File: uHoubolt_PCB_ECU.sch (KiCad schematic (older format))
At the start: 88 parts, among them J1 Power In, J2 Debug, J3 CAN1, J4 CAN2, J5 CAN1, J6 CAN2, U1 SiC431C, U2 TS30041-M050QFNR, U3 MCP1700-3302E, U4 MCP2562FDT-H_SN, U5 MCP2562FDT, U6 STM32G491MET6-LQFP80, U7 ICM-20602, U8 W25Q256JV, X1 TXC-7C

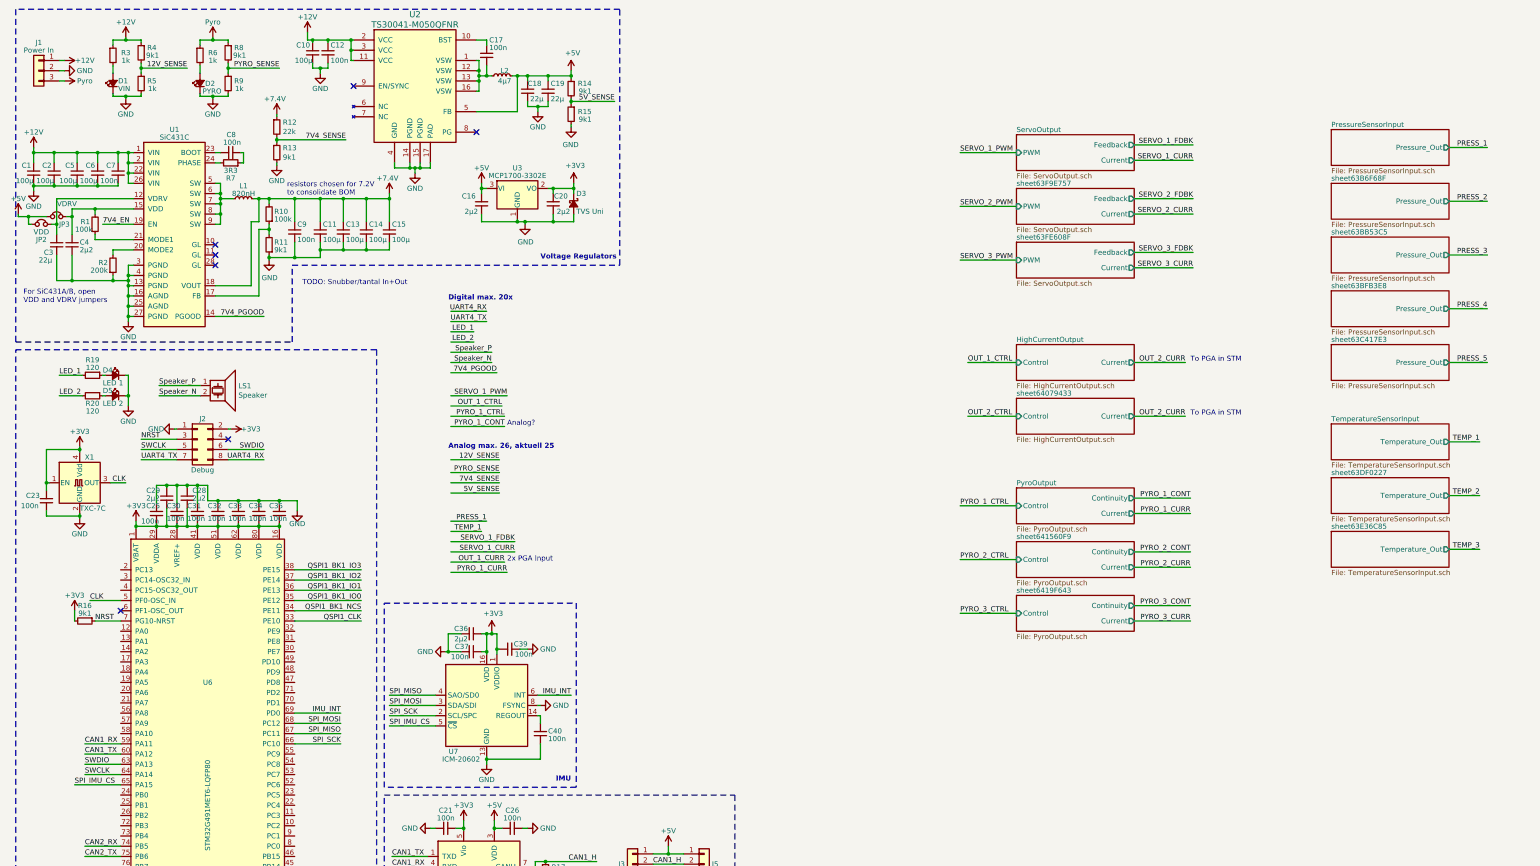
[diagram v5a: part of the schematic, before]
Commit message: moved 7V4 buck to separate board
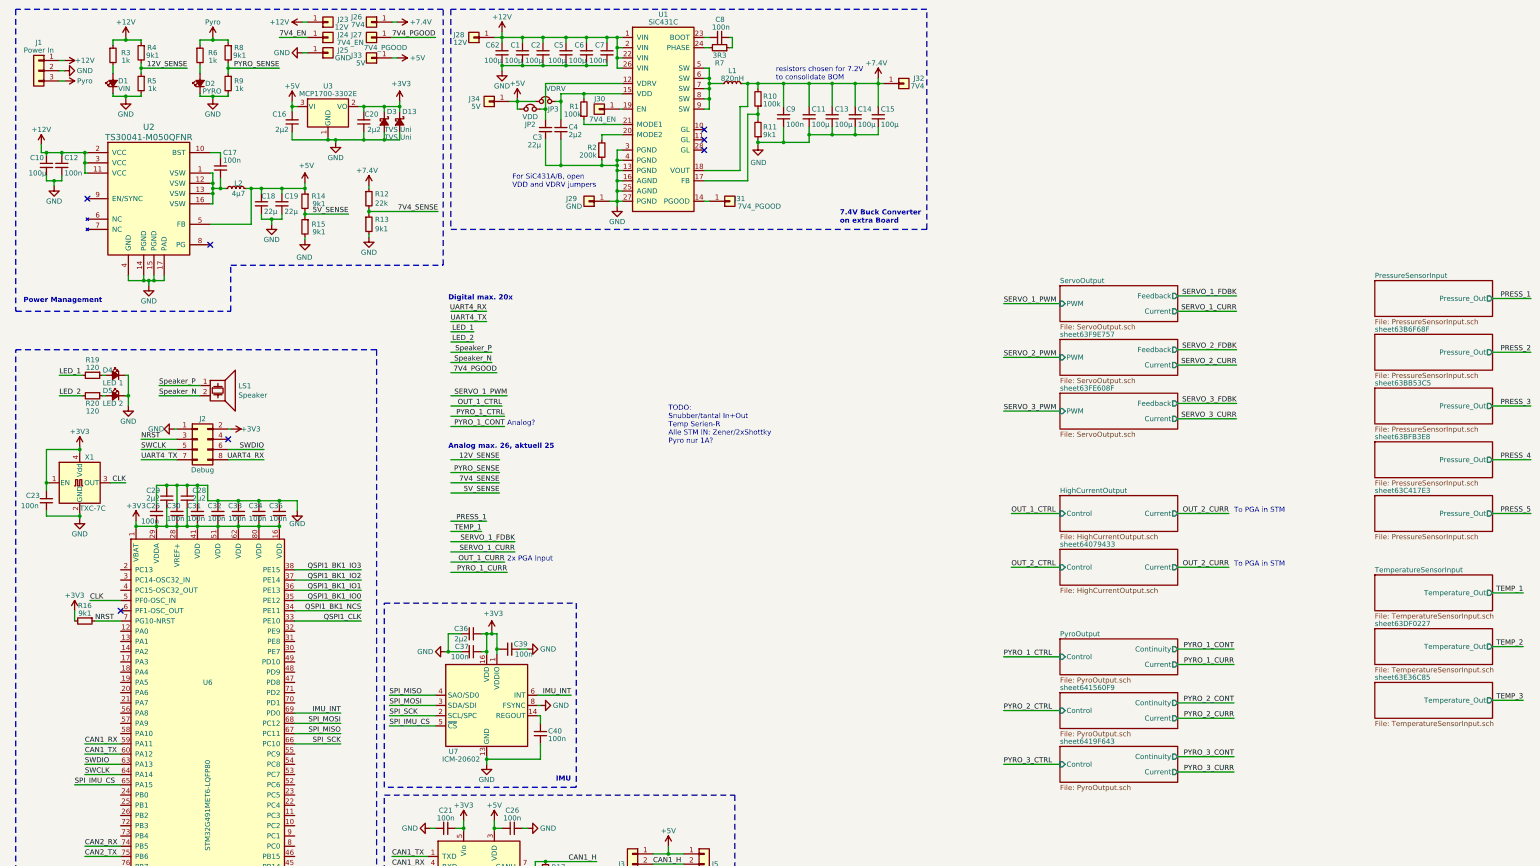
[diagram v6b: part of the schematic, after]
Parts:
- added C62: 100µ, Capacitor_SMD:C_1210_3225Metric, symbol Device:C_Small
- added D13: TVS Uni, TXV_LIB:SOD882D, symbol Device:D_Schottky_Small_ALT
- added J23: 12V, TXV_LIB:PlatedEdgePad_6mm, symbol Connector_Generic:Conn_01x01
- added J24: 7V4_EN, TXV_LIB:PlatedEdgePad_3mm, symbol Connector_Generic:Conn_01x01
- added J25: GND, TXV_LIB:PlatedEdgePad_6mm, symbol Connector_Generic:Conn_01x01
- added J26: 7V4, TXV_LIB:PlatedEdgePad_6mm, symbol Connector_Generic:Conn_01x01
- added J27: 7V4_PGOOD, TXV_LIB:PlatedEdgePad_3mm, symbol Connector_Generic:Conn_01x01
- added J28: 12V, TXV_LIB:PlatedEdge_6mm, symbol Connector_Generic:Conn_01x01
- added J29: GND, TXV_LIB:PlatedEdge_6mm, symbol Connector_Generic:Conn_01x01
- added J30: 7V4_EN, TXV_LIB:PlatedEdge_3mm, symbol Connector_Generic:Conn_01x01
- added J31: 7V4_PGOOD, TXV_LIB:PlatedEdge_3mm, symbol Connector_Generic:Conn_01x01
- added J32: 7V4, TXV_LIB:PlatedEdge_6mm, symbol Connector_Generic:Conn_01x01
- added J33: 5V, TXV_LIB:PlatedEdgePad_3mm, symbol Connector_Generic:Conn_01x01
- added J34: 5V, TXV_LIB:PlatedEdge_3mm, symbol Connector_Generic:Conn_01x01
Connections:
- wire segments 506 -> 523
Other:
- note added: "7.4V Buck Converter\non extra Board"
- note added: "Power Management"
- note added: "TODO:\nSnubber/tantal In+Out\nTemp Serien-R\nAlle STM IN: Zener/2xShottky\nPyro nur 1A?"
- note removed: "TODO: Snubber/tantal In+Out"
- note removed: "Voltage Regulators"
- moved on the sheet: C1, C10, C11, C12, C13, C14, C15, C16, C17, C18, C19, C2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

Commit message: many small changes, before removing servo buck converter
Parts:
- added F?: <1A, symbol Device:Polyfuse_Small
- added J35, J37: CAN1, Connector_JST:JST_GH_BM04B-GHS-TBT_1x04-1MP_P1.25mm_Vertical, symbol Connector_Generic_MountingPin:Conn_01x04_MountingPin
- added J36, J38: CAN2, Connector_JST:JST_GH_BM04B-GHS-TBT_1x04-1MP_P1.25mm_Vertical, symbol Connector_Generic_MountingPin:Conn_01x04_MountingPin
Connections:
- net labels added: 5V_PGOOD, 5V_unfused
- wire segments 523 -> 580
- no-connect marks 7 -> 6
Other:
- note added: "Analog max. 26, aktuell 22"
- note added: "Digital max. 20, aktuell 19"
- note added: "TODO:\nKleinerer L?\nSnubber/tantal In+Out\nAlle STM IN: 2x Shottky\nAnderer Speaker\n6. Druck?\nServo LEDs?\nLEDs 7V4, 5V, 3V3?\nnach außen gehende 12V Versorgungen absichern (vor Messung)"
- note removed: "Analog max. 26, aktuell 25"
- note removed: "Analog?"
- note removed: "Digital max. 20x"
- note removed: "TODO:\nSnubber/tantal In+Out\nTemp Serien-R\nAlle STM IN: Zener/2xShottky\nPyro nur 1A?"
- moved on the sheet: C21, C22, C23, C25, C26, C27, C28, C29, C30, C31, C32, C33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

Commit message: placement almost done
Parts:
- removed C1, C11, C13, C14, C15, C2, C5, C6, C62: 100µ, Capacitor_SMD:C_1210_3225Metric, symbol Device:C_Small
- removed C3: 22µ, Capacitor_SMD:C_0603_1608Metric, symbol Device:C_Small
- removed C4: 2µ2, Capacitor_SMD:C_0603_1608Metric, symbol Device:C_Small
- removed C7, C8, C9: 100n, Capacitor_SMD:C_0402_1005Metric, symbol Device:C_Small
- removed D3: TVS Uni, Diode_SMD:D_SOD-123F, symbol Device:D_Schottky_Small_ALT
- removed J23: 12V, TXV_LIB:PlatedEdgePad_6mm, symbol Connector_Generic:Conn_01x01
- removed J27: 7V4_PGOOD, TXV_LIB:PlatedEdgePad_3mm, symbol Connector_Generic:Conn_01x01
- removed J28: 12V, TXV_LIB:PlatedEdge_6mm, symbol Connector_Generic:Conn_01x01
- removed J29: GND, TXV_LIB:PlatedEdge_6mm, symbol Connector_Generic:Conn_01x01
- removed J30: 7V4_EN, TXV_LIB:PlatedEdge_3mm, symbol Connector_Generic:Conn_01x01
- removed J31: 7V4_PGOOD, TXV_LIB:PlatedEdge_3mm, symbol Connector_Generic:Conn_01x01
- removed J32: 7V4, TXV_LIB:PlatedEdge_6mm, symbol Connector_Generic:Conn_01x01
- removed J33: 5V, TXV_LIB:PlatedEdgePad_3mm, symbol Connector_Generic:Conn_01x01
- removed J34: 5V, TXV_LIB:PlatedEdge_3mm, symbol Connector_Generic:Conn_01x01
- removed JP2: VDD, Jumper:SolderJumper-2_P1.3mm_Bridged_RoundedPad1.0x1.5mm, symbol Device:Jumper_NC_Small
- removed JP3: VDRV, Jumper:SolderJumper-2_P1.3mm_Bridged_RoundedPad1.0x1.5mm, symbol Device:Jumper_NC_Small
- removed L1: 820nH, Inductor_SMD:L_Vishay_IHLP-6767, symbol Device:L_Small
- removed R1, R10: 100k, Resistor_SMD:R_0603_1608Metric, symbol Device:R_Small
- removed R11: 9k1, Resistor_SMD:R_0603_1608Metric, symbol Device:R_Small
- removed R2: 200k, Resistor_SMD:R_0603_1608Metric, symbol Device:R_Small
- removed R7: 3R3, Resistor_SMD:R_0603_1608Metric, symbol Device:R_Small
- removed U1: SiC431C, TXV_LIB:SiC431AEDT1GE3, symbol TXV_LIB:SiC431CED-T1-GE3
- added D17: 3V3, LED_SMD:LED_0603_1608Metric, symbol Device:LED_Small_ALT
- added D3: 5V, LED_SMD:LED_0603_1608Metric, symbol Device:LED_Small_ALT
- added F2: 350mA, Fuse:Fuse_1206_3216Metric, symbol Device:Polyfuse_Small
- added R75, R76: 1k, Resistor_SMD:R_0603_1608Metric, symbol Device:R_Small
- added U20: D1213A-04V, Package_TO_SOT_SMD:SOT-563, symbol TXV_LIB:D1213A-04V
- C10: value 100µ -> 10µ; footprint Capacitor_SMD:C_1210_3225Metric -> Capacitor_SMD:C_0805_2012Metric
- D13: value TVS Uni -> TVS 3V3
- F1: renamed from F?; value <1A -> 350mA; footprint (none) -> Fuse:Fuse_1206_3216Metric
- J24: value 7V4_EN -> 12V; footprint TXV_LIB:PlatedEdgePad_3mm -> TXV_LIB:PlatedEdgePad_6mm
- J26: value 7V4 -> Servo
- R12: value 22k -> 9k1
- R13: value 9k1 -> 1k
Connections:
- net labels added: +12VA, 12VA_SENSE, PRESS_6, SERVO_1_LED, SERVO_2_LED, SERVO_3_LED, UART_RX, UART_TX, VS
- net labels removed: +7.4V, 7V4_EN, 7V4_PGOOD, 7V4_SENSE, UART4_RX, UART4_TX
- wire segments 580 -> 484
- no-connect marks 6 -> 3
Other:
- note added: "Analog max. 26"
- note added: "Digital max. 20"
- note added: "TODO:\nAlle STM IN: 2x Shottky\n0 indiziert, richtige zuordnung zu netzen und values"
- note removed: "7.4V Buck Converter\non extra Board"
- note removed: "Analog max. 26, aktuell 22"
- note removed: "Digital max. 20, aktuell 19"
- note removed: "For SiC431A/B, open\nVDD and VDRV jumpers"
- note removed: "TODO:\nKleinerer L?\nSnubber/tantal In+Out\nAlle STM IN: 2x Shottky\nAnderer Speaker\n6. Druck?\nServo LEDs?\nLEDs 7V4, 5V, 3V3?\nnach außen gehende 12V Versorgungen absichern (vor Messung)"
- note removed: "resistors chosen for 7.2V\nto consolidate BOM"
- moved on the sheet: D13
